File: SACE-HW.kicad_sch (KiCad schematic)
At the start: 0 parts

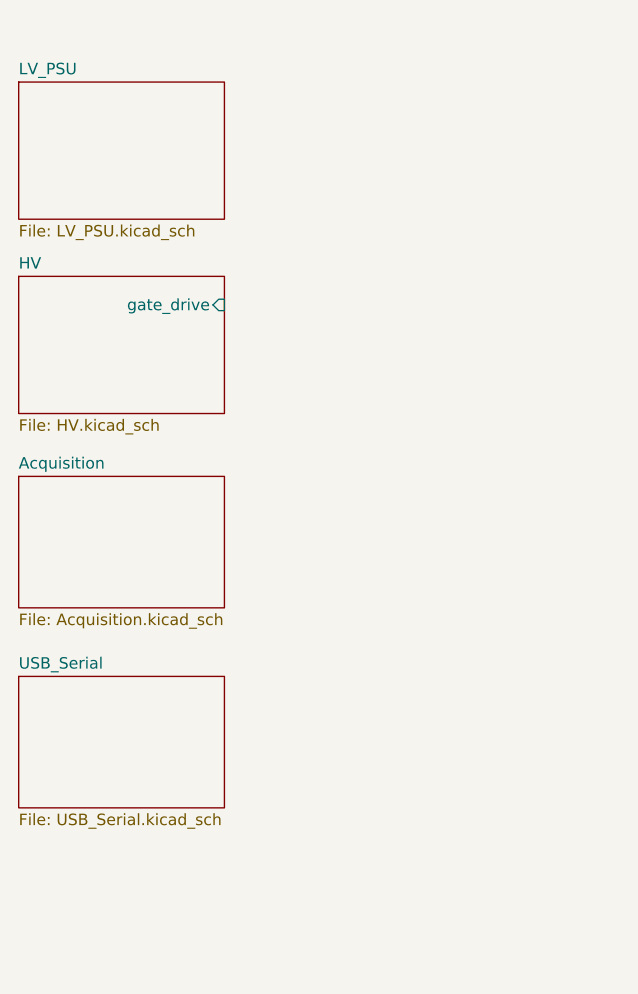
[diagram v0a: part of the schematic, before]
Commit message: update schematic
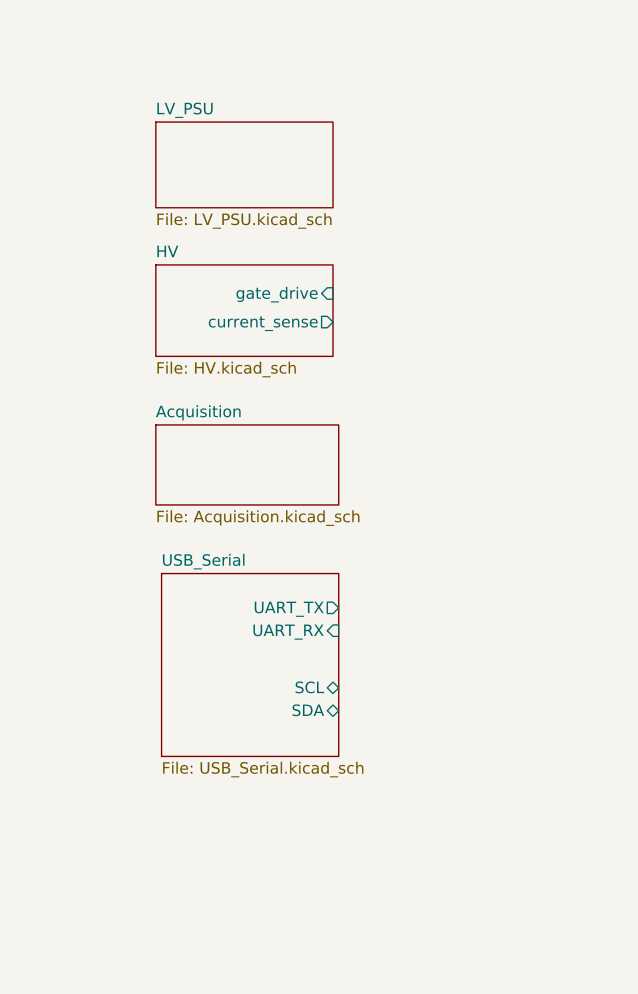
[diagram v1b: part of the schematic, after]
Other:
- sheet HV ports: added current_sense; removed none
- sheet USB_Serial ports: added SCL, SDA, UART_RX, UART_TX; removed none
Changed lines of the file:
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@@
 	)
 	(sheet
-		(at 143.51 27.94)
-		(size 22.86 15.24)
+		(at 158.75 32.385)
+		(size 19.685 9.525)
 		(fields_autoplaced yes)
 		(stroke
@@
 		)
 		(property "Sheetname" "LV_PSU"
-			(at 143.51 27.2284 0)
+			(at 158.75 31.6734 0)
 			(effects
 				(font
@@
 		)
 		(property "Sheetfile" "LV_PSU.kicad_sch"
-			(at 143.51 43.7646 0)
+			(at 158.75 42.4946 0)
 			(effects
 				(font
@@
 	)
 	(sheet
-		(at 143.51 71.755)
-		(size 22.86 14.605)
+		(at 158.75 66.04)
+		(size 20.32 8.89)
 		(fields_autoplaced yes)
 		(stroke
@@
 		)
 		(property "Sheetname" "Acquisition"
-			(at 143.51 71.0434 0)
+			(at 158.75 65.3284 0)
 			(effects
 				(font
@@
 		)
 		(property "Sheetfile" "Acquisition.kicad_sch"
-			(at 143.51 86.9446 0)
+			(at 158.75 75.5146 0)
 			(effects
 				(font
@@
 	)
 	(sheet
-		(at 143.51 93.98)
-		(size 22.86 14.605)
+		(at 159.385 82.55)
+		(size 19.685 20.32)
 		(fields_autoplaced yes)
 		(stroke
@@
 		)
 		(property "Sheetname" "USB_Serial"
-			(at 143.51 93.2684 0)
+			(at 159.385 81.8384 0)
 			(effects
 				(font
@@
 		)
 		(property "Sheetfile" "USB_Serial.kicad_sch"
-			(at 143.51 109.1696 0)
+			(at 159.385 103.4546 0)
 			(effects
 				(font
@@
 				)
 				(justify left top)
+			)
+		)
+		(pin "UART_TX" output
+			(at 179.07 86.36 0)
+			(effects
+				(font
+					(size 1.27 1.27)
+				)
+				(justify right)
+			)
+		)
+		(pin "UART_RX" input
+			(at 179.07 88.9 0)
+			(effects
+				(font
+					(size 1.27 1.27)
+				)
+				(justify right)
+			)
+		)
+		(pin "SCL" bidirectional
+			(at 179.07 95.25 0)
+			(effects
+				(font
+					(size 1.27 1.27)
+				)
+				(justify right)
+			)
+		)
+		(pin "SDA" bidirectional
+			(at 179.07 97.79 0)
+			(effects
+				(font
+					(size 1.27 1.27)
+				)
+				(justify right)
 			)
 		)
@@
 	)
 	(sheet
-		(at 143.51 49.53)
-		(size 22.86 15.24)
+		(at 158.75 48.26)
+		(size 19.685 10.16)
 		(fields_autoplaced yes)
 		(stroke
@@
 		)
 		(property "Sheetname" "HV"
-			(at 143.51 48.8184 0)
+			(at 158.75 47.5484 0)
 			(effects
 				(font
@@
 		)
 		(property "Sheetfile" "HV.kicad_sch"
-			(at 143.51 65.3546 0)
+			(at 158.75 59.0046 0)
 			(effects
 				(font
@@
 		)
 		(pin "gate_drive" input
-			(at 166.37 52.705 0)
-			(effects
-				(font
+			(at 178.435 51.435 0)
+			(effects
+				(font
+					(size 1.27 1.27)
+				)
+				(justify right)
+			)
+		)
+		(pin "current_sense" output
+			(at 178.435 54.61 0)
+			(effects
+				(font

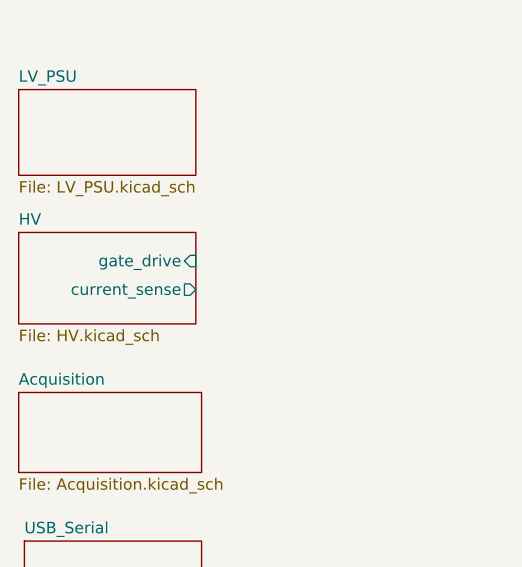
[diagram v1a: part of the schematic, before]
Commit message: update schematic
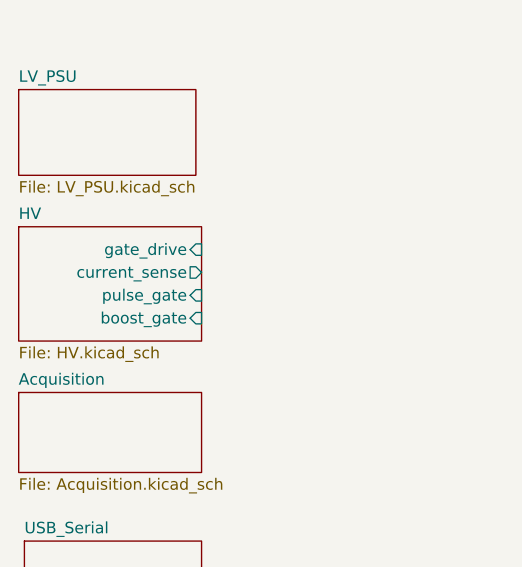
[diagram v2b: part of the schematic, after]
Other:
- sheet HV ports: added boost_gate, pulse_gate; removed none
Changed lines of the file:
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@@
 	)
 	(sheet
-		(at 158.75 48.26)
-		(size 19.685 10.16)
+		(at 158.75 47.625)
+		(size 20.32 12.7)
 		(fields_autoplaced yes)
 		(stroke
@@
 		)
 		(property "Sheetname" "HV"
-			(at 158.75 47.5484 0)
+			(at 158.75 46.9134 0)
 			(effects
 				(font
@@
 		)
 		(property "Sheetfile" "HV.kicad_sch"
-			(at 158.75 59.0046 0)
+			(at 158.75 60.9096 0)
 			(effects
 				(font
@@
 		)
 		(pin "gate_drive" input
-			(at 178.435 51.435 0)
+			(at 179.07 50.165 0)
 			(effects
 				(font
@@
 		)
 		(pin "current_sense" output
-			(at 178.435 54.61 0)
+			(at 179.07 52.705 0)
 			(effects
 				(font
+					(size 1.27 1.27)
+				)
+				(justify right)
+			)
+		)
+		(pin "pulse_gate" input
+			(at 179.07 55.245 0)
+			(effects
+				(font
+					(size 1.27 1.27)
+				)
+				(justify right)
+			)
+		)
+		(pin "boost_gate" input
+			(at 179.07 57.785 0)
+			(effects
+				(font

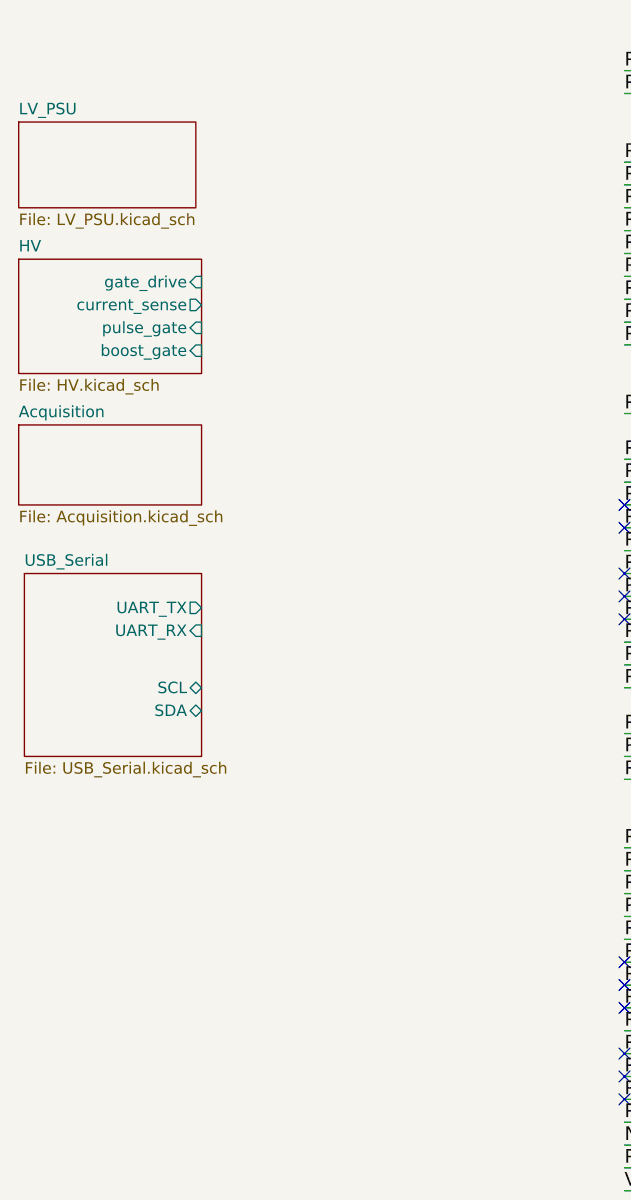
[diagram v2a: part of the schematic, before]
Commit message: update schematic
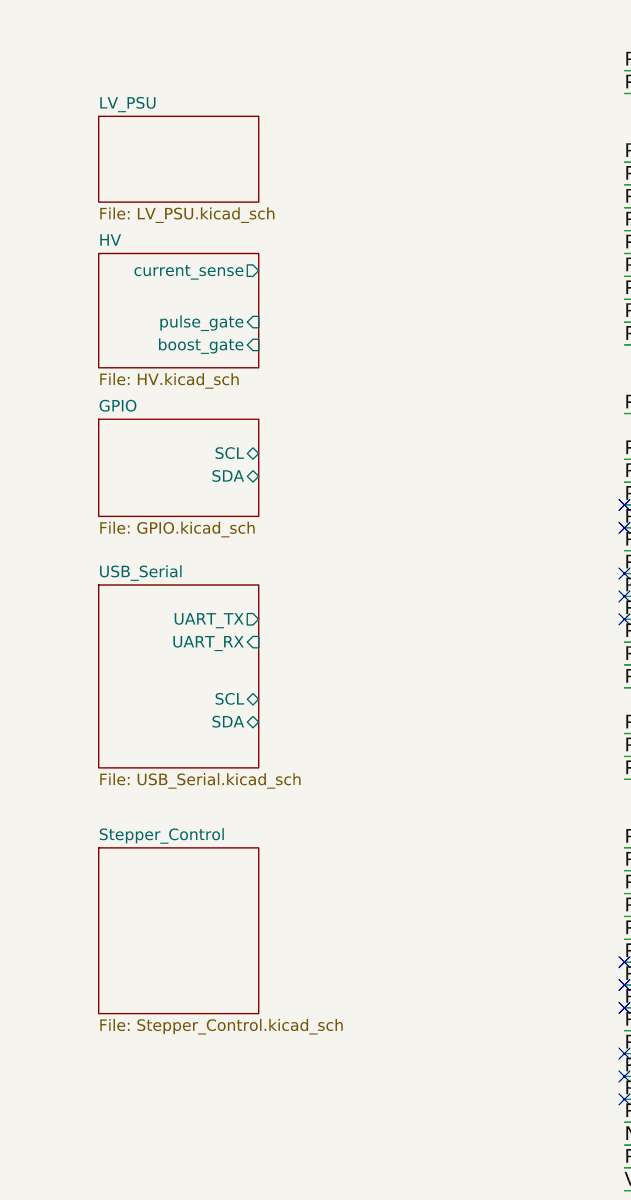
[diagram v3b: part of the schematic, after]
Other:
- sheet Acquisition renamed GPIO
- added sheet Stepper_Control (Stepper_Control.kicad_sch)
- sheet GPIO: file Acquisition.kicad_sch -> GPIO.kicad_sch
- sheet GPIO ports: added SCL, SDA; removed none
- sheet HV ports: added none; removed gate_drive
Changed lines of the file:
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@@
 	)
 	(sheet
-		(at 158.75 32.385)
-		(size 19.685 9.525)
+		(at 167.64 31.75)
+		(size 17.78 9.525)
 		(fields_autoplaced yes)
 		(stroke
@@
 		)
 		(property "Sheetname" "LV_PSU"
-			(at 158.75 31.6734 0)
+			(at 167.64 31.0384 0)
 			(effects
 				(font
@@
 		)
 		(property "Sheetfile" "LV_PSU.kicad_sch"
-			(at 158.75 42.4946 0)
+			(at 167.64 41.8596 0)
 			(effects
 				(font
@@
 				(path "/4c1e5ca8-aa0f-4a8e-bffe-6765adb2e3e8"
 					(page "2")
+				)
+			)
+		)
+	)
+	(sheet
+		(at 167.64 113.03)
+		(size 17.78 18.415)
+		(fields_autoplaced yes)
+		(stroke
+			(width 0.1524)
+			(type solid)
+		)
+		(fill
+			(color 0 0 0 0.0000)
+		)
+		(property "Sheetname" "Stepper_Control"
+			(at 167.64 112.3184 0)
+			(effects
+				(font
+					(size 1.27 1.27)
+				)
+				(justify left bottom)
+			)
+		)
+		(property "Sheetfile" "Stepper_Control.kicad_sch"
+			(at 167.64 132.0296 0)
+			(effects
+				(font
+					(size 1.27 1.27)
+				)
+				(justify left top)
+			)
+		)
+		(instances
+			(project "SACE-HW"
+				(path "/4c1e5ca8-aa0f-4a8e-bffe-6765adb2e3e8"
+					(page "7")
 				)
 			)
@@
 	)
 	(sheet
-		(at 158.75 66.04)
-		(size 20.32 8.89)
+		(at 167.64 65.405)
+		(size 17.78 10.795)
 		(fields_autoplaced yes)
 		(stroke
@@
 			(color 0 0 0 0.0000)
 		)
-		(property "Sheetname" "Acquisition"
-			(at 158.75 65.3284 0)
+		(property "Sheetname" "GPIO"
+			(at 167.64 64.6934 0)
 			(effects
 				(font
@@
 			)
 		)
-		(property "Sheetfile" "Acquisition.kicad_sch"
-			(at 158.75 75.5146 0)
+		(property "Sheetfile" "GPIO.kicad_sch"
+			(at 167.64 76.7846 0)
 			(effects
 				(font
@@
 				)
 				(justify left top)
+			)
+		)
+		(pin "SCL" bidirectional
+			(at 185.42 69.215 0)
+			(effects
+				(font
+					(size 1.27 1.27)
+				)
+				(justify right)
+			)
+		)
+		(pin "SDA" bidirectional
+			(at 185.42 71.755 0)
+			(effects
+				(font
+					(size 1.27 1.27)
+				)
+				(justify right)
 			)
 		)
@@
 	)
 	(sheet
-		(at 159.385 82.55)
-		(size 19.685 20.32)
+		(at 167.64 83.82)
+		(size 17.78 20.32)
 		(fields_autoplaced yes)
 		(stroke
@@
 		)
 		(property "Sheetname" "USB_Serial"
-			(at 159.385 81.8384 0)
+			(at 167.64 83.1084 0)
 			(effects
 				(font
@@
 		)
 		(property "Sheetfile" "USB_Serial.kicad_sch"
-			(at 159.385 103.4546 0)
+			(at 167.64 104.7246 0)
 			(effects
 				(font
@@
 		)
 		(pin "UART_TX" output
-			(at 179.07 86.36 0)
+			(at 185.42 87.63 0)
 			(effects
 				(font
@@
 		)
 		(pin "UART_RX" input
-			(at 179.07 88.9 0)
+			(at 185.42 90.17 0)
 			(effects
 				(font
@@
 		)
 		(pin "SCL" bidirectional
-			(at 179.07 95.25 0)
+			(at 185.42 96.52 0)
 			(effects
 				(font
@@
 		)
 		(pin "SDA" bidirectional
-			(at 179.07 97.79 0)
+			(at 185.42 99.06 0)
 			(effects
 				(font
@@
 	)
 	(sheet
-		(at 158.75 47.625)
-		(size 20.32 12.7)
+		(at 167.64 46.99)
+		(size 17.78 12.7)
 		(fields_autoplaced yes)
 		(stroke
@@
 		)
 		(property "Sheetname" "HV"
-			(at 158.75 46.9134 0)
+			(at 167.64 46.2784 0)
 			(effects
 				(font
@@
 		)
 		(property "Sheetfile" "HV.kicad_sch"
-			(at 158.75 60.9096 0)
+			(at 167.64 60.2746 0)
 			(effects
 				(font
@@
 			)
 		)
-		(pin "gate_drive" input
-			(at 179.07 50.165 0)
-			(effects
-				(font
-					(size 1.27 1.27)
-				)
-				(justify right)
-			)
-		)
 		(pin "current_sense" output
-			(at 179.07 52.705 0)
+			(at 185.42 48.895 0)
 			(effects
 				(font
@@
 		)
 		(pin "pulse_gate" input
-			(at 179.07 55.245 0)
+			(at 185.42 54.61 0)
 			(effects
 				(font
@@
 		)
 		(pin "boost_gate" input
-			(at 179.07 57.785 0)
-			(effects
-				(font
+			(at 185.42 57.15 0)
+			(effects
+				(font

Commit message: modif schématique
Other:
- sheet GPIO renamed 5V_LOGIC_I2C
- sheet 5V_LOGIC_I2C: file GPIO.kicad_sch -> 5V_LOGIC_I2C.kicad_sch
- sheet 5V_LOGIC_I2C ports: added SCL_3_3, SDA_3_3; removed SCL, SDA
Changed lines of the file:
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@@
 			(color 0 0 0 0.0000)
 		)
-		(property "Sheetname" "GPIO"
+		(property "Sheetname" "5V_LOGIC_I2C"
 			(at 167.64 64.6934 0)
 			(effects
@@
 			)
 		)
-		(property "Sheetfile" "GPIO.kicad_sch"
+		(property "Sheetfile" "5V_LOGIC_I2C.kicad_sch"
 			(at 167.64 76.7846 0)
 			(effects
@@
 			)
 		)
-		(pin "SCL" bidirectional
-			(at 185.42 69.215 0)
+		(pin "SCL_3_3" bidirectional
+			(at 185.42 72.39 0)
 			(effects
 				(font
@@
 			)
 		)
-		(pin "SDA" bidirectional
-			(at 185.42 71.755 0)
+		(pin "SDA_3_3" bidirectional
+			(at 185.42 68.58 0)
 			(effects
 				(font

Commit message: update schematique
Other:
- sheet 5V_LOGIC_I2C renamed I2C
- sheet I2C: file 5V_LOGIC_I2C.kicad_sch -> I2C.kicad_sch
- sheet I2C ports: added SCL, SDA; removed SCL_3_3, SDA_3_3
- sheet USB_Serial ports: added RST_, USB_ID, USB_VBUS; removed none
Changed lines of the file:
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@@
 	)
 	(sheet
-		(at 167.64 113.03)
+		(at 167.64 124.46)
 		(size 17.78 18.415)
 		(fields_autoplaced yes)
@@
 		)
 		(property "Sheetname" "Stepper_Control"
-			(at 167.64 112.3184 0)
+			(at 167.64 123.7484 0)
 			(effects
 				(font
@@
 		)
 		(property "Sheetfile" "Stepper_Control.kicad_sch"
-			(at 167.64 132.0296 0)
+			(at 167.64 143.4596 0)
 			(effects
 				(font
@@
 	(sheet
 		(at 167.64 65.405)
-		(size 17.78 10.795)
+		(size 17.78 9.525)
 		(fields_autoplaced yes)
 		(stroke
@@
 			(color 0 0 0 0.0000)
 		)
-		(property "Sheetname" "5V_LOGIC_I2C"
+		(property "Sheetname" "I2C"
 			(at 167.64 64.6934 0)
 			(effects
@@
 			)
 		)
-		(property "Sheetfile" "5V_LOGIC_I2C.kicad_sch"
-			(at 167.64 76.7846 0)
+		(property "Sheetfile" "I2C.kicad_sch"
+			(at 167.64 75.5146 0)
 			(effects
 				(font
@@
 			)
 		)
-		(pin "SCL_3_3" bidirectional
+		(pin "SDA" bidirectional
+			(at 185.42 68.58 0)
+			(effects
+				(font
+					(size 1.27 1.27)
+				)
+				(justify right)
+			)
+		)
+		(pin "SCL" bidirectional
 			(at 185.42 72.39 0)
-			(effects
-				(font
-					(size 1.27 1.27)
-				)
-				(justify right)
-			)
-		)
-		(pin "SDA_3_3" bidirectional
-			(at 185.42 68.58 0)
 			(effects
 				(font
@@
 	(sheet
 		(at 167.64 83.82)
-		(size 17.78 20.32)
+		(size 17.78 30.48)
 		(fields_autoplaced yes)
 		(stroke
@@
 		)
 		(property "Sheetfile" "USB_Serial.kicad_sch"
-			(at 167.64 104.7246 0)
+			(at 167.64 114.8846 0)
 			(effects
 				(font
@@
 		)
 		(pin "SCL" bidirectional
-			(at 185.42 96.52 0)
+			(at 185.42 95.25 0)
 			(effects
 				(font
@@
 		)
 		(pin "SDA" bidirectional
-			(at 185.42 99.06 0)
-			(effects
-				(font
+			(at 185.42 97.79 0)
+			(effects
+				(font
+					(size 1.27 1.27)
+				)
+				(justify right)
+			)
+		)
+		(pin "USB_ID" bidirectional
+			(at 185.42 102.87 0)
+			(effects
+				(font
+					(size 1.27 1.27)
+				)
+				(justify right)
+			)
+		)
+		(pin "RST_" input
+			(at 185.42 107.95 0)
+			(effects
+				(font
+					(size 1.27 1.27)
+				)
+				(justify right)
+			)
+		)
+		(pin "USB_VBUS" bidirectional
+			(at 185.42 111.76 0)
+			(effects
+				(font

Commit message: update schematique
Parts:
- added H101, H102, H103, H104: Mounting-Hole-M3, Connectors:Mounting_Hole_3mm, symbol Mechanicals:Mounting-Hole-M3
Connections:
- no-connect marks 11 -> 4
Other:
- sheet Stepper_Control renamed 5V_OUTPUT
- added sheet POWER_CTRL (POWER_CTRL.kicad_sch)
- added sheet SD_CARD (SD_CARD.kicad_sch)
- sheet 5V_OUTPUT: file Stepper_Control.kicad_sch -> 5V_OUTPUT.kicad_sch
- sheet 5V_OUTPUT ports: added OUT0, OUT1, OUT2, OUT3, OUT4, OUT5, OUT6, OUT7; removed none
- sheet HV ports: added none; removed boost_gate
- title: SACE Hybride 2024 -> SACE 2024
